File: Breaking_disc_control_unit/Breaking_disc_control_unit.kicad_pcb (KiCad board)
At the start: 2 copper layers, 68 parts, among them J1 Conn_02x05_Odd_Even, J2 Conn_02x03_Odd_Even, J3 Conn_01x02, J4 Conn_01x04, J5 Conn_01x03, SW1 SW_Push, U1 MKW31Z256VHT4, U2 TLV4964, U3 MMA8452Q, U4 MPL3115A2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

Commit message: ADC added
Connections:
- U1 pad 24: Net-(U1-Pad24) -> +BATT
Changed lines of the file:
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@@
 (kicad_pcb (version 4) (host pcbnew 4.0.7)
   (general
-    (links 203)
-    (no_connects 191)
-    (area 81.574999 60.995 215.249998 106.525)
+    (links 204)
+    (no_connects 192)
+    (area 0 0 0 0)
     (thickness 1.6)
     (drawings 12)
@@
     (zones 0)
     (modules 68)
-    (nets 60)
+    (nets 59)
   )
   (page A4)
@@
   (net 41 I2C_INT_11)
   (net 42 I2C_INT_12)
-  (net 43 "Net-(U1-Pad24)")
-  (net 44 "Net-(U1-Pad25)")
-  (net 45 "Net-(U1-Pad29)")
-  (net 46 SM_BIN2/BENBL)
-  (net 47 SM_AIN2/AENBL)
-  (net 48 SM_BIN1/BP)
-  (net 49 SM_AIN1/AP)
-  (net 50 I2C_INT_21)
-  (net 51 I2C_INT_22)
-  (net 52 SM_MODE)
-  (net 53 "Net-(U3-Pad13)")
-  (net 54 "Net-(U3-Pad16)")
-  (net 55 "Net-(U3-Pad15)")
-  (net 56 "Net-(U3-Pad3)")
-  (net 57 "Net-(U3-Pad8)")
-  (net 58 "Net-(U5-Pad4)")
-  (net 59 "Net-(AE1-Pad1)")
+  (net 43 "Net-(U1-Pad25)")
+  (net 44 "Net-(U1-Pad29)")
+  (net 45 SM_BIN2/BENBL)
+  (net 46 SM_AIN2/AENBL)
+  (net 47 SM_BIN1/BP)
+  (net 48 SM_AIN1/AP)
+  (net 49 I2C_INT_21)
+  (net 50 I2C_INT_22)
+  (net 51 SM_MODE)
+  (net 52 "Net-(U3-Pad13)")
+  (net 53 "Net-(U3-Pad16)")
+  (net 54 "Net-(U3-Pad15)")
+  (net 55 "Net-(U3-Pad3)")
+  (net 56 "Net-(U3-Pad8)")
+  (net 57 "Net-(U5-Pad4)")
+  (net 58 "Net-(AE1-Pad1)")
   (net_class Default "This is the default net class."
     (clearance 0.2)
@@
     (add_net "Net-(U1-Pad11)")
     (add_net "Net-(U1-Pad12)")
-    (add_net "Net-(U1-Pad24)")
     (add_net "Net-(U1-Pad25)")
     (add_net "Net-(U1-Pad29)")
@@
       (xy -13.635863 -3.47192) (xy -1.716765 -3.45046)) (layer F.Cu) (width 0.01))
     (pad 1 smd rect (at 2.71 3.22) (size 0.85 0.85) (layers F.Cu F.Paste F.Mask)
-      (net 59 "Net-(AE1-Pad1)"))
+      (net 58 "Net-(AE1-Pad1)"))
     (pad 0 smd rect (at 8.73 4.32) (size 3 1) (layers F.Cu F.Paste F.Mask))
   )
@@
     (fp_poly (pts (xy 0 0) (xy 0 -0.25) (xy 0 0)) (layer F.Cu) (width 0.15))
     (pad 1 smd trapezoid (at 0 0) (size 0.6 1.4) (rect_delta 0 -0.3 ) (layers F.Cu)
-      (net 59 "Net-(AE1-Pad1)"))
+      (net 58 "Net-(AE1-Pad1)"))
   )
   (module Capacitors_SMD:C_0402_NoSilk (layer F.Cu)
@@
       (net 1 GND))
     (pad 2 smd rect (at 0.55 0 180) (size 0.6 0.5) (layers F.Cu F.Paste F.Mask)
-      (net 59 "Net-(AE1-Pad1)"))
+      (net 58 "Net-(AE1-Pad1)"))
     (model Capacitors_SMD.3dshapes/C_0402.wrl
       (at (xyz 0 0 0))
@@
       (net 14 "Net-(C30-Pad2)"))
     (pad 2 smd rect (at 0.55 0 90) (size 0.6 0.5) (layers F.Cu F.Paste F.Mask)
-      (net 59 "Net-(AE1-Pad1)"))
+      (net 58 "Net-(AE1-Pad1)"))
     (model Capacitors_SMD.3dshapes/C_0402.wrl
       (at (xyz 0 0 0))
@@
       (net 38 LED))
     (pad 24 smd rect (at 2.75 3.4 90) (size 0.7 0.25) (layers F.Cu F.Paste F.Mask)
-      (net 43 "Net-(U1-Pad24)") (clearance 0.15))
+      (net 2 +BATT) (clearance 0.15))
     (pad 25 smd rect (at 3.4 2.75) (size 0.7 0.25) (layers F.Cu F.Paste F.Mask)
-      (net 44 "Net-(U1-Pad25)") (clearance 0.15))
+      (net 43 "Net-(U1-Pad25)") (clearance 0.15))
     (pad 26 smd rect (at 3.4 2.25) (size 0.7 0.25) (layers F.Cu F.Paste F.Mask)
       (net 1 GND))
@@
       (net 3 +3V3))
     (pad 29 smd rect (at 3.4 0.75) (size 0.7 0.25) (layers F.Cu F.Paste F.Mask)
-      (net 45 "Net-(U1-Pad29)"))
+      (net 44 "Net-(U1-Pad29)"))
     (pad 30 smd rect (at 3.4 0.25) (size 0.7 0.25) (layers F.Cu F.Paste F.Mask)
       (net 10 EXTAL_32MHZ))
@@
       (net 18 UART0_TX))
     (pad 40 smd rect (at 1.25 -3.4 90) (size 0.7 0.25) (layers F.Cu F.Paste F.Mask)
-      (net 46 SM_BIN2/BENBL))
+      (net 45 SM_BIN2/BENBL))
     (pad 41 smd rect (at 0.75 -3.4 90) (size 0.7 0.25) (layers F.Cu F.Paste F.Mask)
-      (net 47 SM_AIN2/AENBL))
+      (net 46 SM_AIN2/AENBL))
     (pad 42 smd rect (at 0.25 -3.4 90) (size 0.7 0.25) (layers F.Cu F.Paste F.Mask)
-      (net 48 SM_BIN1/BP))
+      (net 47 SM_BIN1/BP))
     (pad 43 smd rect (at -0.25 -3.4 90) (size 0.7 0.25) (layers F.Cu F.Paste F.Mask)
-      (net 49 SM_AIN1/AP))
+      (net 48 SM_AIN1/AP))
     (pad 44 smd rect (at -0.75 -3.4 90) (size 0.7 0.25) (layers F.Cu F.Paste F.Mask)
       (net 3 +3V3))
@@
       (net 32 PWM_SERVO))
     (pad 46 smd rect (at -1.75 -3.4 90) (size 0.7 0.25) (layers F.Cu F.Paste F.Mask)
-      (net 50 I2C_INT_21))
+      (net 49 I2C_INT_21))
     (pad 47 smd rect (at -2.25 -3.4 90) (size 0.7 0.25) (layers F.Cu F.Paste F.Mask)
-      (net 51 I2C_INT_22))
+      (net 50 I2C_INT_22))
     (pad 48 smd rect (at -2.75 -3.4 90) (size 0.7 0.25) (layers F.Cu F.Paste F.Mask)
-      (net 52 SM_MODE) (clearance 0.15))
+      (net 51 SM_MODE) (clearance 0.15))
     (pad 50 smd rect (at -0.5 -1.5) (size 0.41 0.41) (layers F.Cu F.Paste F.Mask)
       (net 1 GND) (solder_paste_margin_ratio -0.2))
@@
       (net 3 +3V3))
     (pad 13 smd rect (at 1.275 -1 90) (size 0.305 0.813) (layers F.Cu F.Paste F.Mask)
-      (net 53 "Net-(U3-Pad13)"))
+      (net 52 "Net-(U3-Pad13)"))
     (pad 16 smd rect (at -0.5 -1.275) (size 0.305 0.813) (layers F.Cu F.Paste F.Mask)
-      (net 54 "Net-(U3-Pad16)"))
+      (net 53 "Net-(U3-Pad16)"))
     (pad 15 smd rect (at 0 -1.275) (size 0.305 0.813) (layers F.Cu F.Paste F.Mask)
-      (net 55 "Net-(U3-Pad15)"))
+      (net 54 "Net-(U3-Pad15)"))
     (pad 14 smd rect (at 0.5 -1.275) (size 0.305 0.813) (layers F.Cu F.Paste F.Mask)
       (net 3 +3V3))
@@
       (net 6 "Net-(C15-Pad1)"))
     (pad 3 smd rect (at -1.275 0 90) (size 0.305 0.813) (layers F.Cu F.Paste F.Mask)
-      (net 56 "Net-(U3-Pad3)"))
+      (net 55 "Net-(U3-Pad3)"))
     (pad 4 smd rect (at -1.275 0.5 90) (size 0.305 0.813) (layers F.Cu F.Paste F.Mask)
       (net 36 I2C_SCL))
@@
       (net 1 GND))
     (pad 8 smd rect (at 0.5 1.275) (size 0.305 0.813) (layers F.Cu F.Paste F.Mask)
-      (net 57 "Net-(U3-Pad8)"))
+      (net 56 "Net-(U3-Pad8)"))
   )
   (module Footprint_library:FP_MPL3115 (layer F.Cu)
@@
       (net 35 I2C_SDA))
     (pad 6 smd rect (at 1.025 0.625) (size 1.05 0.55) (layers F.Cu F.Paste F.Mask)
-      (net 50 I2C_INT_21))
+      (net 49 I2C_INT_21))
     (pad 5 smd rect (at 1.025 1.875) (size 1.05 0.55) (layers F.Cu F.Paste F.Mask)
-      (net 51 I2C_INT_22))
+      (net 50 I2C_INT_22))
   )
   (module Footprint_library:LTC3106_TSSOP-20_4.4x6.5mm_Pitch0.65mm (layer F.Cu)
@@
       (net 3 +3V3))
     (pad 4 smd rect (at -2.95 -0.975) (size 1.45 0.45) (layers F.Cu F.Paste F.Mask)
-      (net 58 "Net-(U5-Pad4)"))
+      (net 57 "Net-(U5-Pad4)"))
     (pad 5 smd rect (at -2.95 -0.325) (size 1.45 0.45) (layers F.Cu F.Paste F.Mask)
       (net 7 "Net-(C16-Pad1)"))
@@
       (net 1 GND))
     (pad 7 smd rect (at 0.95 1.25 270) (size 0.5 0.25) (layers F.Cu F.Paste F.Mask)
-      (net 46 SM_BIN2/BENBL))
+      (net 45 SM_BIN2/BENBL))
     (pad 8 smd rect (at 0.95 0.75 270) (size 0.5 0.25) (layers F.Cu F.Paste F.Mask)
-      (net 48 SM_BIN1/BP))
+      (net 47 SM_BIN1/BP))
     (pad 9 smd rect (at 0.95 0.25 270) (size 0.5 0.25) (layers F.Cu F.Paste F.Mask)
-      (net 47 SM_AIN2/AENBL))
+      (net 46 SM_AIN2/AENBL))
     (pad 10 smd rect (at 0.95 -0.25 270) (size 0.5 0.25) (layers F.Cu F.Paste F.Mask)
-      (net 49 SM_AIN1/AP))
+      (net 48 SM_AIN1/AP))
     (pad 11 smd rect (at 0.95 -0.75 270) (size 0.5 0.25) (layers F.Cu F.Paste F.Mask)
-      (net 52 SM_MODE))
+      (net 51 SM_MODE))
     (pad 12 smd rect (at 0.95 -1.25 270) (size 0.5 0.25) (layers F.Cu F.Paste F.Mask)
       (net 3 +3V3))
@@
   (segment (start 155.35 88.9) (end 157.3 88.9) (width 0.3) (layer F.Cu) (net 15))
   (segment (start 157.3 88.9) (end 157.95 88.9) (width 0.3) (layer F.Cu) (net 15))
-  (segment (start 161.3 82.35) (end 161.3 83.45) (width 0.3) (layer F.Cu) (net 59))
-  (segment (start 161.3 82.35) (end 161.3 80.7) (width 0.3) (layer F.Cu) (net 59))
-  (segment (start 161.3 80.7) (end 161.31 80.69) (width 0.3) (layer F.Cu) (net 59))
-  (segment (start 161.31 80.69) (end 161.31 79.62) (width 0.3) (layer F.Cu) (net 59))
-  (segment (start 161.3 79.63) (end 161.31 79.62) (width 0.3) (layer F.Cu) (net 59))
-  (segment (start 161.35 80.85) (end 161.3 80.8) (width 0.3) (layer F.Cu) (net 59))
+  (segment (start 161.3 82.35) (end 161.3 83.45) (width 0.3) (layer F.Cu) (net 58))
+  (segment (start 161.3 82.35) (end 161.3 80.7) (width 0.3) (layer F.Cu) (net 58))
+  (segment (start 161.3 80.7) (end 161.31 80.69) (width 0.3) (layer F.Cu) (net 58))
+  (segment (start 161.31 80.69) (end 161.31 79.62) (width 0.3) (layer F.Cu) (net 58))
+  (segment (start 161.3 79.63) (end 161.31 79.62) (width 0.3) (layer F.Cu) (net 58))
+  (segment (start 161.35 80.85) (end 161.3 80.8) (width 0.3) (layer F.Cu) (net 58))
   (zone (net 0) (net_name "") (layer F.Cu) (hatch edge 0.508)
     (connect_pads (clearance 0.508))

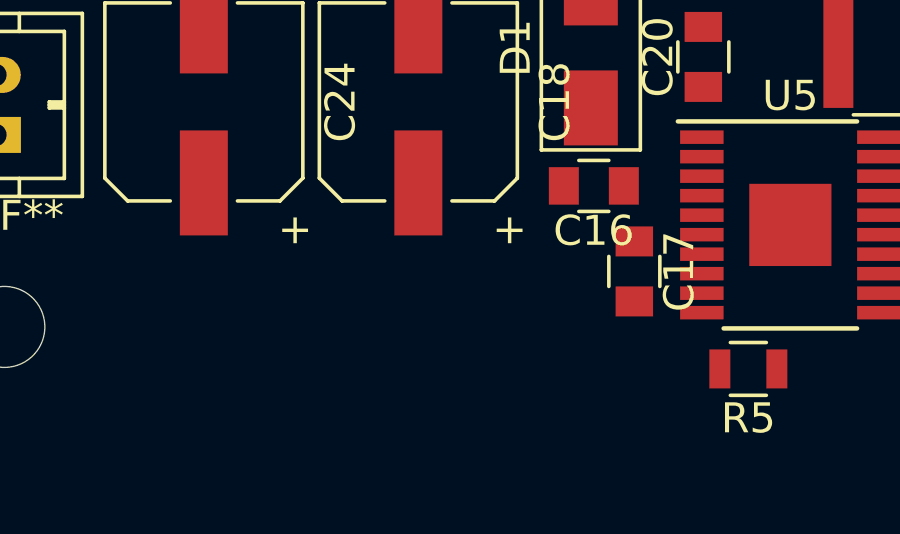
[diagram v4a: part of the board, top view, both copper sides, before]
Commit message: Diode for ADC added
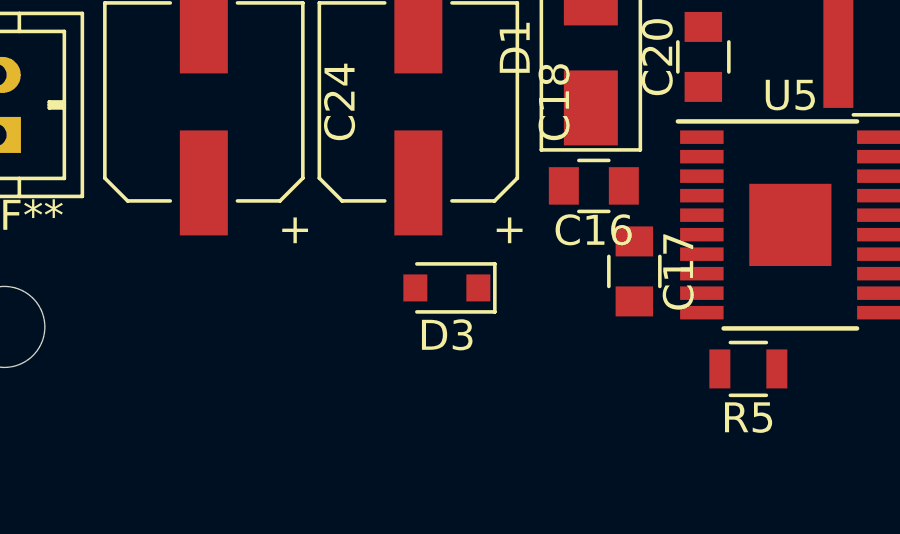
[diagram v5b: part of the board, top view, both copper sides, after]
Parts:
- added D3: D, Diodes_SMD:D_0805, F.Cu at (101.0, 100.2)
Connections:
- U1 pad 24: +BATT -> Net-(D3-Pad1)
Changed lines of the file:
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@@
 (kicad_pcb (version 4) (host pcbnew 4.0.7)
   (general
-    (links 204)
-    (no_connects 192)
+    (links 205)
+    (no_connects 193)
     (area 0 0 0 0)
     (thickness 1.6)
@@
     (tracks 23)
     (zones 0)
-    (modules 68)
-    (nets 59)
+    (modules 69)
+    (nets 60)
   )
   (page A4)
@@
   (net 57 "Net-(U5-Pad4)")
   (net 58 "Net-(AE1-Pad1)")
+  (net 59 "Net-(D3-Pad1)")
   (net_class Default "This is the default net class."
     (clearance 0.2)
@@
     (add_net "Net-(D1-Pad2)")
     (add_net "Net-(D2-Pad2)")
+    (add_net "Net-(D3-Pad1)")
     (add_net "Net-(J1-Pad5)")
     (add_net "Net-(J1-Pad6)")
@@
       (net 38 LED))
     (pad 24 smd rect (at 2.75 3.4 90) (size 0.7 0.25) (layers F.Cu F.Paste F.Mask)
-      (net 2 +BATT) (clearance 0.15))
+      (net 59 "Net-(D3-Pad1)") (clearance 0.15))
     (pad 25 smd rect (at 3.4 2.75) (size 0.7 0.25) (layers F.Cu F.Paste F.Mask)
       (net 43 "Net-(U1-Pad25)") (clearance 0.15))
@@
     (pad "" np_thru_hole circle (at 0 0) (size 2.7 2.7) (drill 2.7) (layers *.Cu *.Mask))
   )
+  (module Diodes_SMD:D_0805 (layer F.Cu)
+    (at 100.95 100.2 180)
+    (descr "Diode SMD in 0805 package http://datasheets.avx.com/schottky.pdf")
+    (tags "smd diode")
+    (attr smd)
+    (fp_text reference D3 (at 0 -1.6 180) (layer F.SilkS)
+      (effects (font (size 1 1) (thickness 0.15)))
+    )
+    (fp_text value D (at 0 1.7 180) (layer F.Fab)
+      (effects (font (size 1 1) (thickness 0.15)))
+    )
+    (fp_text user %R (at 0 -1.6 180) (layer F.Fab)
+      (effects (font (size 1 1) (thickness 0.15)))
+    )
+    (fp_line (start -1.6 -0.8) (end -1.6 0.8) (layer F.SilkS) (width 0.12))
+    (fp_line (start -1.7 0.88) (end -1.7 -0.88) (layer F.CrtYd) (width 0.05))
+    (fp_line (start 1.7 0.88) (end -1.7 0.88) (layer F.CrtYd) (width 0.05))
+    (fp_line (start 1.7 -0.88) (end 1.7 0.88) (layer F.CrtYd) (width 0.05))
+    (fp_line (start -1.7 -0.88) (end 1.7 -0.88) (layer F.CrtYd) (width 0.05))
+    (fp_line (start 0.2 0) (end 0.4 0) (layer F.Fab) (width 0.1))
+    (fp_line (start -0.1 0) (end -0.3 0) (layer F.Fab) (width 0.1))
+    (fp_line (start -0.1 -0.2) (end -0.1 0.2) (layer F.Fab) (width 0.1))
+    (fp_line (start 0.2 0.2) (end 0.2 -0.2) (layer F.Fab) (width 0.1))
+    (fp_line (start -0.1 0) (end 0.2 0.2) (layer F.Fab) (width 0.1))
+    (fp_line (start 0.2 -0.2) (end -0.1 0) (layer F.Fab) (width 0.1))
+    (fp_line (start -1 0.65) (end -1 -0.65) (layer F.Fab) (width 0.1))
+    (fp_line (start 1 0.65) (end -1 0.65) (layer F.Fab) (width 0.1))
+    (fp_line (start 1 -0.65) (end 1 0.65) (layer F.Fab) (width 0.1))
+    (fp_line (start -1 -0.65) (end 1 -0.65) (layer F.Fab) (width 0.1))
+    (fp_line (start -1.6 0.8) (end 1 0.8) (layer F.SilkS) (width 0.12))
+    (fp_line (start -1.6 -0.8) (end 1 -0.8) (layer F.SilkS) (width 0.12))
+    (pad 1 smd rect (at -1.05 0 180) (size 0.8 0.9) (layers F.Cu F.Paste F.Mask)
+      (net 59 "Net-(D3-Pad1)"))
+    (pad 2 smd rect (at 1.05 0 180) (size 0.8 0.9) (layers F.Cu F.Paste F.Mask)
+      (net 2 +BATT))
+    (model ${KISYS3DMOD}/Diodes_SMD.3dshapes/D_0805.wrl
+      (at (xyz 0 0 0))
+      (scale (xyz 1 1 1))
+      (rotate (xyz 0 0 0))
+    )
+  )
   (dimension 90.200014 (width 0.3) (layer F.Fab)

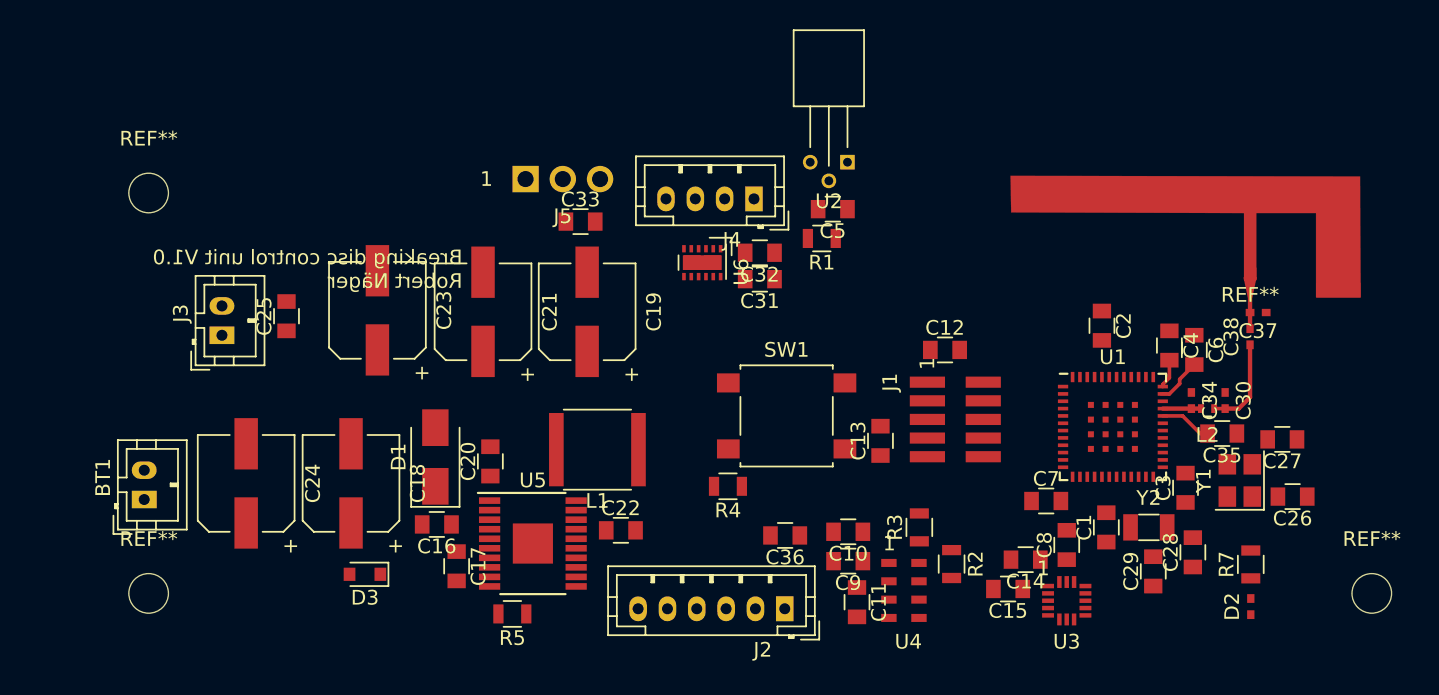
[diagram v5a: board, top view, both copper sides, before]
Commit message: Changed Antenna -> Must be matched after measuring and started layouting
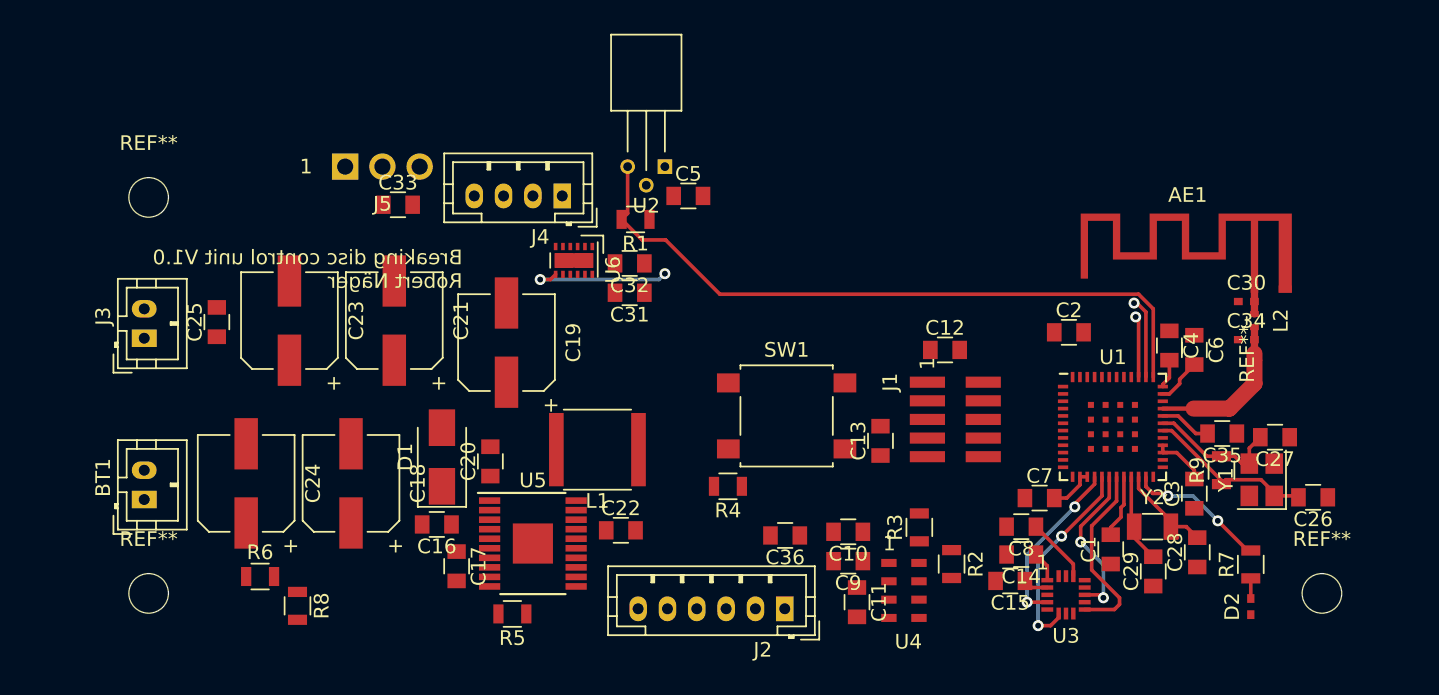
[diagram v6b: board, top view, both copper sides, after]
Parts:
- removed C37: 0.5pF, Capacitors_SMD:C_0402_NoSilk
- removed C38: 1.5pF, Capacitors_SMD:C_0402_NoSilk
- removed D3: D, Diodes_SMD:D_0805
- removed G***: LOGO, Footprint_library:Antenna
- added AE1: MIFA, RF_Antennas:Texas_SWRA117D_2.4GHz_Left, F.Cu at (161.6, 80.8)
- added R6: 2.2M, Resistors_SMD:R_0805, F.Cu at (93.8, 100.3)
- added R8: 4.7M, Resistors_SMD:R_0805, F.Cu at (96.3, 102.3)
- added R9: 1M, Resistors_SMD:R_0805, F.Cu at (159.3, 93.1)
- moved J4 13.1 mm to (114.4, 74.4)
- moved R1 12.8 mm to (119.4, 76.0)
- moved C33 12.5 mm to (103.2, 75.0)
- moved U2 12.5 mm to (121.4, 72.4)
- moved J5 12.3 mm to (99.6, 72.4)
- moved C5 9.89 mm to (123.0, 74.4), turned to 0 degrees
- moved C31 8.92 mm to (119.0, 81.0)
- moved C32 8.90 mm to (119.0, 79.0)
- moved U6 8.75 mm to (115.2, 78.8)
- moved C30 6.90 mm to (161.1, 81.6), turned to 0 degrees
- moved L2 6.80 mm to (161.6, 82.9), turned to 270 degrees
- moved C21 6.08 mm to (103.0, 82.9)
- moved C23 6.04 mm to (95.8, 82.9)
- moved C19 5.89 mm to (110.6, 84.4)
- moved C34 5.59 mm to (161.1, 84.2), turned to 0 degrees
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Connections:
- REF** pad 1: Net-(AE1-Pad1) (its old number) -> Net-(C34-Pad2)
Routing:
- net HALL_OUT: track 0.00 -> 47.2 mm
- net +3V3: track 8.79 -> 26.5 mm
- net I2C_SDA: track 0.00 -> 13.9 mm, vias 0 -> 2
- net I2C_INT_12: track 0.00 -> 12.7 mm
- net EXTAL_32MHZ: track 0.00 -> 11.9 mm
- net I2C_SCL: track 0.00 -> 11.8 mm, vias 0 -> 2
- net I2C_INT_11: track 0.00 -> 11.1 mm, vias 0 -> 2
- net SM_BIN2/BENBL: track 0.00 -> 9.86 mm, vias 0 -> 2
- net LED: track 0.00 -> 9.62 mm, vias 0 -> 2
- net XTAL_32MHZ: track 0.00 -> 9.15 mm
- net Net-(C34-Pad2): track 2.60 -> 10.8 mm
- net XTAL_32KHZ: track 0.00 -> 7.18 mm
- net EXTAL_32KHZ: track 0.00 -> 6.20 mm
- net UART0_RX: track 0.00 -> 5.50 mm, vias 0 -> 1
- net Net-(AE1-Pad1): track 6.38 -> 1.75 mm
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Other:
- net class Default: via_dia 0.6 -> 0.75
- net class Power added: clearance 0.3, trace_width 0.4, via_dia 0.75, via_drill 0.4
- net class RF_trace: trace_width 0.3 -> 0.5; via_dia 0.6 -> 0.75
- net class RF_trace_MCU: via_dia 0.6 -> 0.75
- rule via_min_size: 0.4 -> 0.75
- board text removed: "RF trace width? - 0.85 mm (antenna feed width) - recommended from NXP: 1.3 mm but KW31Z pin is smaller"

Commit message: some tracks
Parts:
- moved R4 5.16 mm to (123.8, 89.4), turned to 270 degrees
- moved C12 2.69 mm to (137.9, 85.6), turned to 180 degrees
- moved C31 1.30 mm to (119.0, 79.7)
- moved C32 0.95 mm to (119.0, 78.0)
- moved R2 0.83 mm to (141.7, 99.8)
- moved C2 0.72 mm to (149.6, 84.1)
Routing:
- net PWM_SERVO: track 0.00 -> 60.3 mm
- net SM_AIN1/AP: track 0.00 -> 45.1 mm, vias 0 -> 2
- net SM_AIN2/AENBL: track 0.00 -> 43.2 mm
- net SM_BIN1/BP: track 0.00 -> 43.2 mm
- net SPI1_SCK_EXT: track 0.00 -> 40.4 mm, vias 0 -> 2
- net SM_MODE: track 0.00 -> 40.1 mm, vias 0 -> 2
- net SPI1_SIN_EXT: track 0.00 -> 37.9 mm, vias 0 -> 2
- net SM_BIN2/BENBL: track 9.86 -> 46.7 mm
- net SPI1_PCS0_EXT: track 0.00 -> 35.6 mm, vias 0 -> 2
- net SPI1_SOUT_EXT: track 0.00 -> 31.8 mm
- net RESET: track 0.00 -> 28.3 mm
- net UART0_RX: track 5.50 -> 24.5 mm, vias 1 -> 2
- net VSOURCE: track 0.00 -> 18.2 mm
- net UART0_TX: track 4.18 -> 18.5 mm, vias 1 -> 2
- net Net-(J4-Pad4): track 0.00 -> 7.92 mm
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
